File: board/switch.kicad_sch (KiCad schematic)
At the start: 2 parts

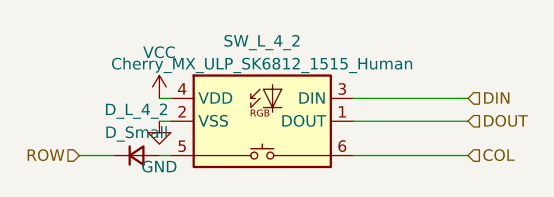
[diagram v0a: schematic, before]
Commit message: changed to 5*4+3+1 layout
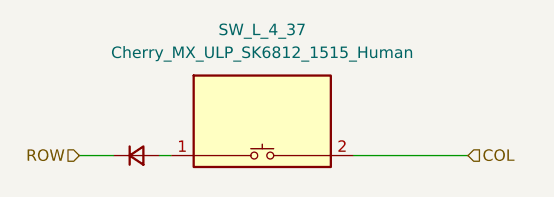
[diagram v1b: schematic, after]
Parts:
- renumbered D_L_4_2 to D_L_4_37, SW_L_4_2 to SW_L_4_37
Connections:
- net DOUT is gone; now on an unnamed net: SW_L_4_37.1
- net GND is gone; now on net COL: SW_L_4_37.2
- net COL: no longer SW_L_4_37.6
- net at D_L_4_37.2 (A): no longer SW_L_4_37.5
- removed net DIN: SW_L_4_37.3 (DIN)
- removed net VCC: SW_L_4_37.4 (VDD)
